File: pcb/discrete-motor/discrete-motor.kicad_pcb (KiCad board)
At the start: 2 copper layers, 96.5 x 66 mm, 20 parts, among them J1 ScrewTerminal, U1 PinHeader8, U2 PinHeader8

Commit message: discrete motor
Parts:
- removed REF** (x4): MountingHole_3.2mm_M3, MountingHole:MountingHole_3.2mm_M3
- added C10: 100n, Capacitor_SMD:C_0603_1608Metric, F.Cu at (81.3, 78.7)
- added C11: 100n, Capacitor_SMD:C_0603_1608Metric, F.Cu at (88.9, 31.8)
- added C12: 100n, Capacitor_SMD:C_0603_1608Metric, F.Cu at (106.7, 78.7)
- added C13: 100n, Capacitor_SMD:C_0603_1608Metric, F.Cu at (113.0, 26.7)
- added CF10: 100n, Capacitor_SMD:C_0603_1608Metric, F.Cu at (68.6, 34.3)
- added CF11: 100n, Capacitor_SMD:C_0603_1608Metric, F.Cu at (94.0, 34.3)
- added CSA10: 100n, Capacitor_SMD:C_0603_1608Metric, F.Cu at (76.2, 31.8)
- added CSA11: 100n, Capacitor_SMD:C_0603_1608Metric, F.Cu at (100.3, 30.5)
- added D10: ~, Diode_SMD:D_SMA, F.Cu at (88.4, 78.7)
- added D11: ~, Diode_SMD:D_SMA, F.Cu at (82.5, 29.2)
- added D12: ~, Diode_SMD:D_SMA, F.Cu at (113.8, 78.7)
- added D13: ~, Diode_SMD:D_SMA, F.Cu at (108.0, 29.2)
- added M1: MountingHole_3.2mm_M3, MountingHole:MountingHole_3.2mm_M3, F.Cu at (30.5, 30.5)
- added M2: MountingHole_3.2mm_M3, MountingHole:MountingHole_3.2mm_M3, F.Cu at (30.5, 86.4)
- added M3: MountingHole_3.2mm_M3, MountingHole:MountingHole_3.2mm_M3, F.Cu at (116.8, 86.4)
- added M4: MountingHole_3.2mm_M3, MountingHole:MountingHole_3.2mm_M3, F.Cu at (116.8, 30.5)
- added QH10: ~, Package_TO_SOT_SMD:TO-263-2, F.Cu at (73.7, 66.0)
- added QH11: ~, Package_TO_SOT_SMD:TO-263-2, F.Cu at (86.4, 48.3)
- added QH12: ~, Package_TO_SOT_SMD:TO-263-2, F.Cu at (99.1, 66.0)
- added QH13: ~, Package_TO_SOT_SMD:TO-263-2, F.Cu at (111.8, 48.3)
- added QL10: ~, Package_TO_SOT_SMD:TO-263-2, F.Cu at (86.4, 66.0)
- added QL11: ~, Package_TO_SOT_SMD:TO-263-2, F.Cu at (73.7, 48.3)
- added QL12: ~, Package_TO_SOT_SMD:TO-263-2, F.Cu at (111.8, 66.0)
- added QL13: ~, Package_TO_SOT_SMD:TO-263-2, F.Cu at (99.1, 48.3)
- added RF10: 1k, Resistor_SMD:R_0603_1608Metric, F.Cu at (68.6, 31.8)
- added RF11: 1k, Resistor_SMD:R_0603_1608Metric, F.Cu at (94.0, 31.8)
- added RH10: 10, Resistor_SMD:R_0603_1608Metric, F.Cu at (71.1, 78.7)
- added RH11: 10, Resistor_SMD:R_0603_1608Metric, F.Cu at (88.9, 35.6)
- added RH12: 10, Resistor_SMD:R_0603_1608Metric, F.Cu at (96.5, 78.7)
- added RH13: 10, Resistor_SMD:R_0603_1608Metric, F.Cu at (114.3, 35.6)
- added RL10: 10, Resistor_SMD:R_0603_1608Metric, F.Cu at (83.8, 78.7)
- added RL11: 10, Resistor_SMD:R_0603_1608Metric, F.Cu at (76.2, 35.6)
- added RL12: 10, Resistor_SMD:R_0603_1608Metric, F.Cu at (109.2, 78.7)
- added RL13: 10, Resistor_SMD:R_0603_1608Metric, F.Cu at (101.6, 35.6)
- added RS10: 10m, Resistor_SMD:R_1206_3216Metric, F.Cu at (72.4, 36.8)
- added RS11: 10m, Resistor_SMD:R_1206_3216Metric, F.Cu at (97.8, 36.8)
- added U10: ~, Package_SO:SOIC-8_3.9x4.9mm_P1.27mm, F.Cu at (76.2, 80.0)
- added U11: ~, Package_SO:SOIC-8_3.9x4.9mm_P1.27mm, F.Cu at (82.5, 34.3)
- added U12: ~, Package_SO:SOIC-8_3.9x4.9mm_P1.27mm, F.Cu at (101.6, 80.0)
- added U13: ~, Package_SO:SOIC-8_3.9x4.9mm_P1.27mm, F.Cu at (108.0, 34.3)
- added UA10: ~, Package_TO_SOT_SMD:SOT-23-6, F.Cu at (72.4, 33.0)
- added UA11: ~, Package_TO_SOT_SMD:SOT-23-6, F.Cu at (97.8, 33.0)
- J1: value ScrewTerminal -> ~
- R1: value ~ -> 4.7k
- R4: value ~ -> 330
- U1, U2: value PinHeader8 -> ~
- moved U4 8.03 mm to (50.8, 55.9)
- moved U3 8.02 mm to (58.4, 35.6)
- moved R1 5.08 mm to (45.7, 33.0)
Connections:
- J4 pad 1: unconnected-(J4-Pin_1-Pad1) -> Net-(J4-Pin_1)
- J4 pad 2: unconnected-(J4-Pin_2-Pad2) -> Net-(J4-Pin_2)
- J4 pad 3: unconnected-(J4-Pin_3-Pad3) -> Net-(J4-Pin_3)
- J4 pad 4: unconnected-(J4-Pin_4-Pad4) -> Net-(J4-Pin_4)
- U1 pad 2: unconnected-(U1-Pin_2-Pad2) -> Net-(U1-Pin_2)
- U1 pad 3: unconnected-(U1-Pin_3-Pad3) -> Net-(U1-Pin_3)
- U1 pad 6: unconnected-(U1-Pin_6-Pad6) -> Net-(U1-Pin_6)
- U1 pad 7: unconnected-(U1-Pin_7-Pad7) -> Net-(U1-Pin_7)
- U1 pad 8: unconnected-(U1-Pin_8-Pad8) -> Net-(U1-Pin_8)
- U2 pad 2: unconnected-(U2-Pin_2-Pad2) -> Net-(U2-Pin_2)
- U2 pad 4: unconnected-(U2-Pin_4-Pad4) -> Net-(U2-Pin_4)
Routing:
- net /12V: track 27.4 -> 251.1 mm, vias 0 -> 6
- net /GND: track 112.2 -> 293.6 mm, vias 0 -> 10
- net Net-(U1-Pin_8): track 0.00 -> 179.0 mm, vias 0 -> 4
- net Net-(J4-Pin_4): track 0.00 -> 105.8 mm, vias 0 -> 6
- net Net-(J4-Pin_2): track 0.00 -> 97.4 mm, vias 0 -> 6
- net /3V3: track 48.4 -> 134.6 mm, vias 1 -> 3
- net Net-(U1-Pin_6): track 0.00 -> 81.2 mm, vias 0 -> 3
- net Net-(QL10-S): track 0.00 -> 72.4 mm, vias 0 -> 5
- net Net-(U1-Pin_7): track 0.00 -> 72.0 mm, vias 0 -> 3
- net Net-(U2-Pin_4): track 0.00 -> 67.0 mm, vias 0 -> 2
- net Net-(QL12-S): track 0.00 -> 67.0 mm, vias 0 -> 4
- net Net-(U1-Pin_3): track 0.00 -> 66.6 mm, vias 0 -> 1
- net Net-(J4-Pin_1): track 0.00 -> 58.8 mm, vias 0 -> 6
- net Net-(U1-Pin_2): track 0.00 -> 57.0 mm, vias 0 -> 1
- net Net-(J4-Pin_3): track 0.00 -> 52.0 mm, vias 0 -> 5
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
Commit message: pcb wip
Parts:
- RH10, RH11, RH12, RH13, RL10, RL11, RL12, RL13: footprint Resistor_SMD:R_0603_1608Metric -> Resistor_SMD:R_0402_1005Metric

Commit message: wip
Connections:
- D10 pad 2: /12V -> /VMOT
- D11 pad 2: /12V -> /VMOT
- D12 pad 2: /12V -> /VMOT
- D13 pad 2: /12V -> /VMOT
- J2 pad 1: unconnected-(J2-Pin_1-Pad1) -> /GND
- J2 pad 2: unconnected-(J2-Pin_2-Pad2) -> /VMOT
- QH10 pad 2: /12V -> /VMOT
- QH11 pad 2: /12V -> /VMOT
- QH12 pad 2: /12V -> /VMOT
- QH13 pad 2: /12V -> /VMOT
- U10 pad 1: /12V -> /VMOT
- U11 pad 1: /12V -> /VMOT
- U12 pad 1: /12V -> /VMOT
- U13 pad 1: /12V -> /VMOT
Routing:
- net /VMOT: track 0.00 -> 236.9 mm, vias 0 -> 6
- net /12V: track 251.1 -> 27.4 mm, vias 6 -> 0
- net /GND: track 293.6 -> 298.7 mm
- net /CANH: track 45.3 -> 44.2 mm, vias 1 -> 0
- net Net-(J4-Pin_1): vias 6 -> 5
- net /CANL: vias 1 -> 0

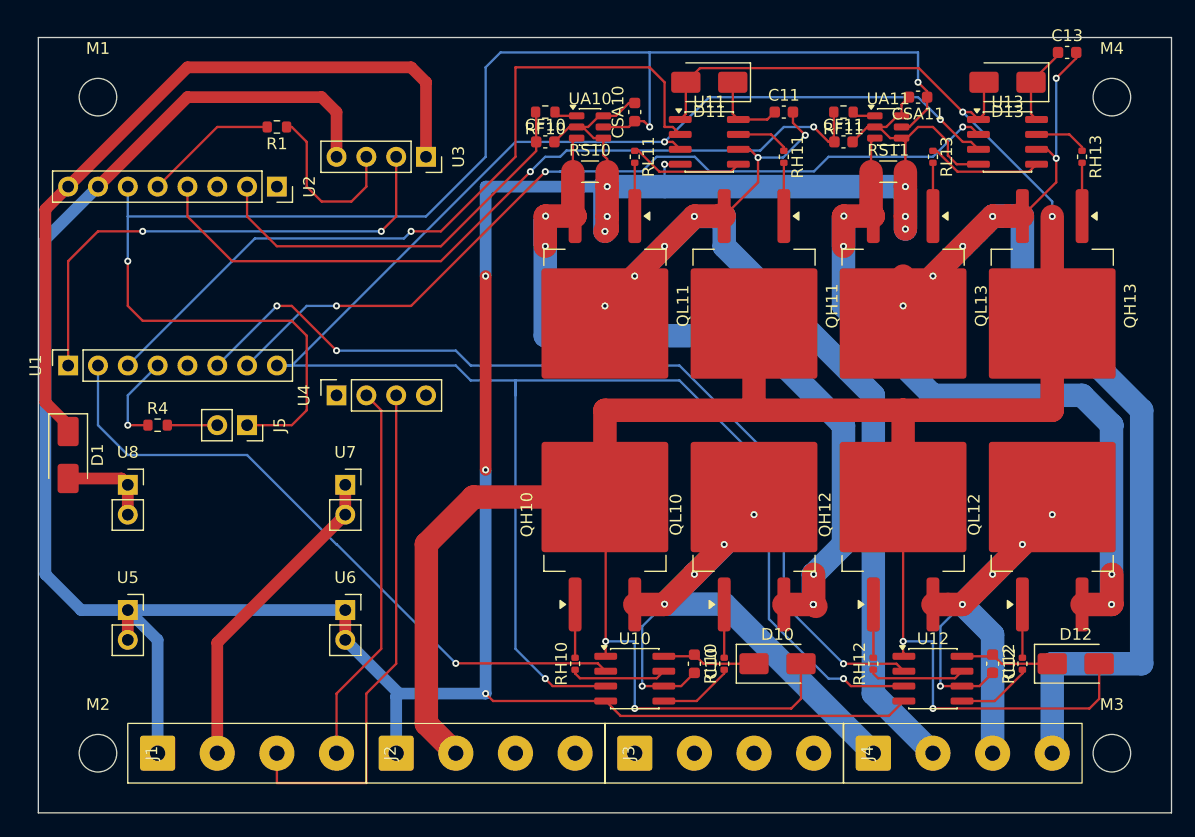
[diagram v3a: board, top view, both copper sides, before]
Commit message: discrete motor fixes
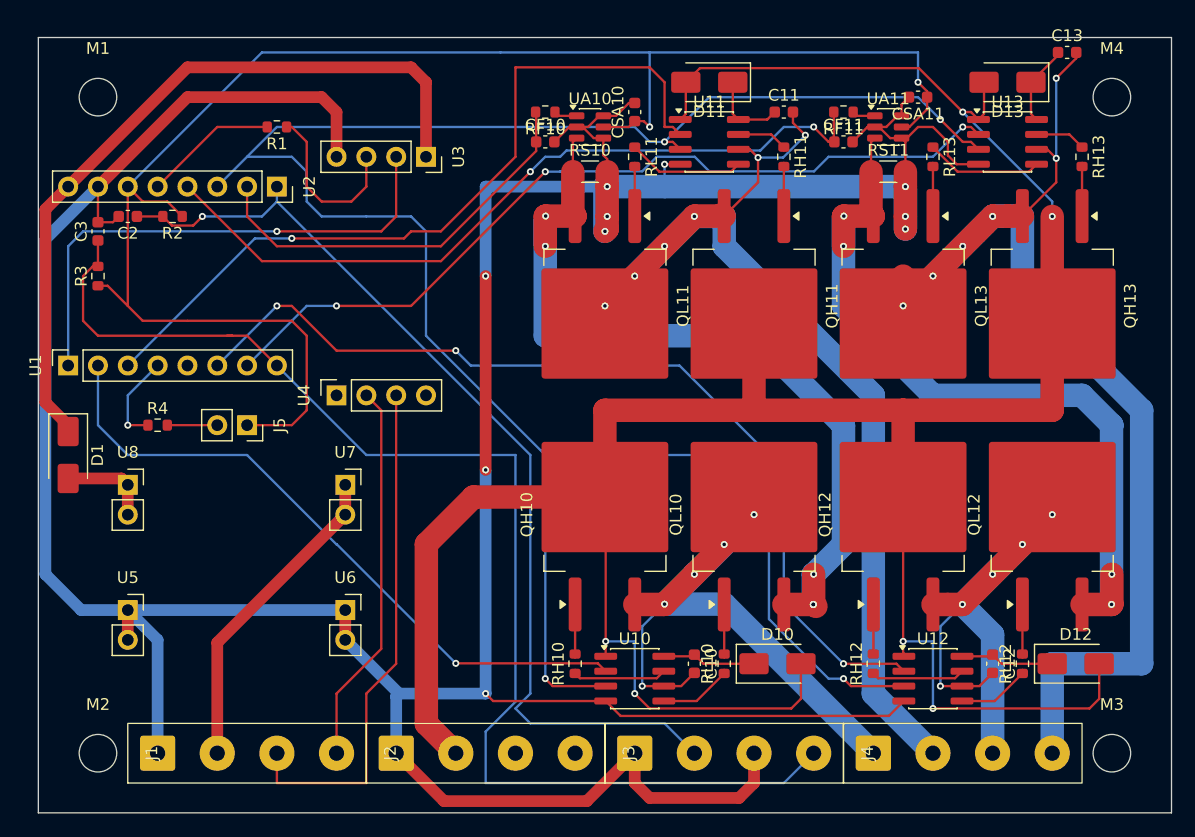
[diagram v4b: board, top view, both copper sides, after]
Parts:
- added C2: 100n, Capacitor_SMD:C_0603_1608Metric, F.Cu at (33.0, 40.6)
- added C3: 100n, Capacitor_SMD:C_0603_1608Metric, F.Cu at (30.5, 41.9)
- added R2: 4.7k, Resistor_SMD:R_0603_1608Metric, F.Cu at (36.8, 40.6)
- added R3: 4.7k, Resistor_SMD:R_0603_1608Metric, F.Cu at (30.5, 45.7)
- RH10, RH11, RH12, RH13, RL10, RL11, RL12, RL13: footprint Resistor_SMD:R_0402_1005Metric -> Resistor_SMD:R_0603_1608Metric
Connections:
- J3 pad 1: unconnected-(J3-Pin_1-Pad1) -> /GND
- J3 pad 2: unconnected-(J3-Pin_2-Pad2) -> Net-(J3-Pin_2)
- J3 pad 3: unconnected-(J3-Pin_3-Pad3) -> /GND
- J3 pad 4: unconnected-(J3-Pin_4-Pad4) -> Net-(J3-Pin_4)
- U1 pad 8: Net-(U1-Pin_8) -> Net-(J3-Pin_4)
- U10 pad 3: Net-(U1-Pin_8) -> Net-(U10-~{SD})
- U11 pad 3: Net-(U1-Pin_8) -> Net-(U10-~{SD})
- U12 pad 3: Net-(U1-Pin_8) -> Net-(U10-~{SD})
- U13 pad 3: Net-(U1-Pin_8) -> Net-(U10-~{SD})
- U2 pad 1: unconnected-(U2-Pin_1-Pad1) -> Net-(J3-Pin_2)
- U2 pad 3: unconnected-(U2-Pin_3-Pad3) -> Net-(U10-~{SD})
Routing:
- net Net-(U10-~{SD}): track 0.00 -> 186.7 mm, vias 0 -> 4
- net Net-(U1-Pin_8): track 179.0 -> 0.00 mm, vias 4 -> 0
- net Net-(J3-Pin_4): track 0.00 -> 107.6 mm
- net Net-(J3-Pin_2): track 0.00 -> 83.8 mm, vias 0 -> 1
- net /GND: track 298.7 -> 343.7 mm
- net /3V3: track 134.6 -> 138.1 mm, vias 3 -> 2
- net Net-(U2-Pin_4): track 67.0 -> 65.6 mm
- net Net-(U1-Pin_1): track 43.5 -> 44.2 mm, vias 2 -> 1
- net /VMOT: track 236.9 -> 236.2 mm
